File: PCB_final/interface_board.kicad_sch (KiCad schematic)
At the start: 114 parts, among them J1 02x30_Shift_Register_Connector, J2 02x30_ADC_Connector, U1 74HC595, U10 LM321, U2 74HC595, U3 74HC595, U4 74HC595, U5 74HC595, U6 74HC595, U7 74HC595, U8 MAX11643EEG, U9 MAX11643EEG

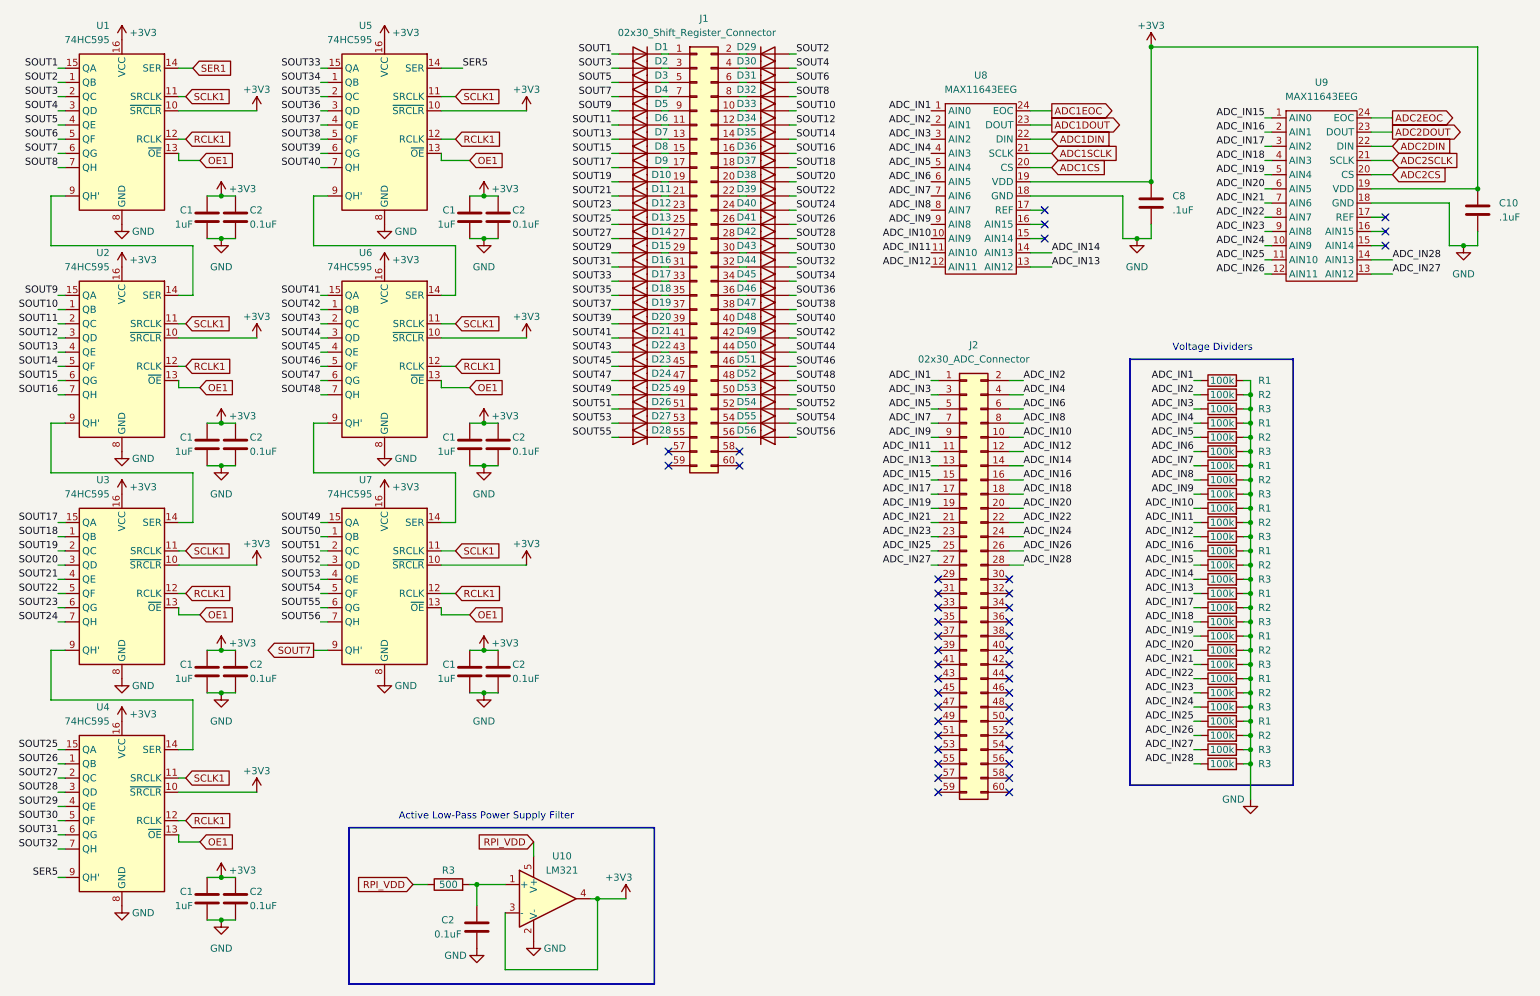
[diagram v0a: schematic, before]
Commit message: Updated op amp and added rpi pico to schematic
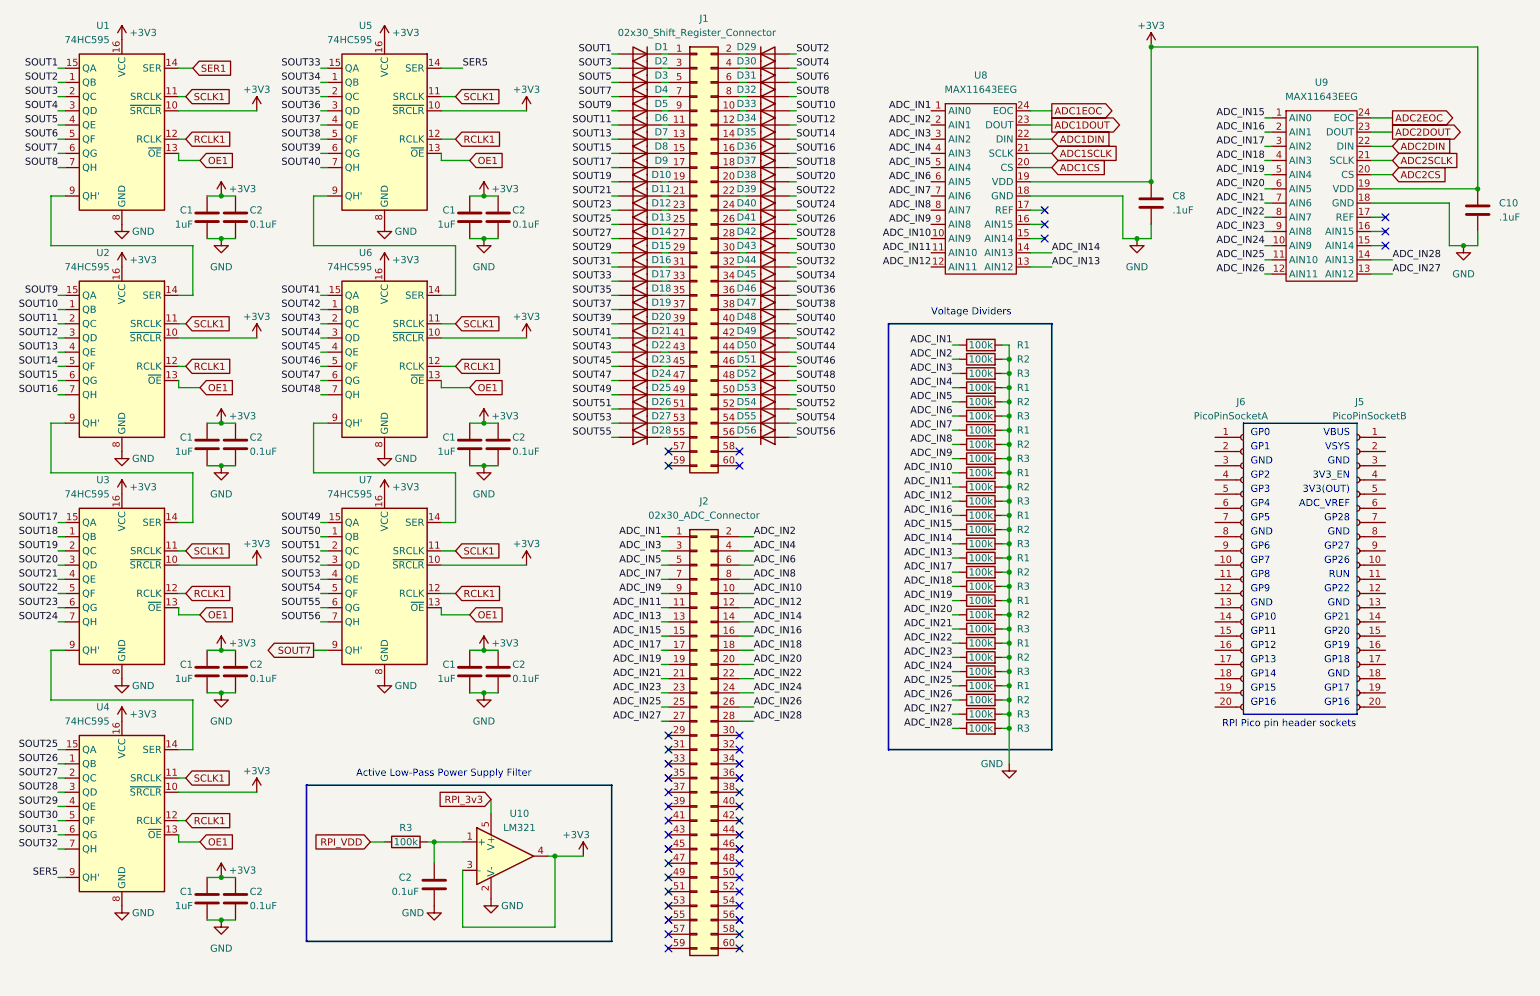
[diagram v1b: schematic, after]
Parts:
- added J5: PicoPinSocketB, symbol Connector:Conn_01x20_Socket
- added J6: PicoPinSocketA, symbol Connector:Conn_01x20_Socket
- R3: value 500 -> 100k
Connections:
- net RPI_VDD: no longer U10.5 (V+)
- new net RPI_3v3: U10.5 (V+)
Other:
- note added: "3V3(OUT)"
- note added: "3V3_EN"
- note added: "ADC_VREF"
- note added: "GND"
- note added: "GP0"
- note added: "GP1"
- note added: "GP10"
- note added: "GP11"
- note added: "GP12"
- note added: "GP13"
- note added: "GP14"
- note added: "GP15"
- note added: "GP16"
- note added: "GP17"
- note added: "GP18"
- note added: "GP19"
- note added: "GP2"
- note added: "GP20"
- note added: "GP21"
- note added: "GP22"
- note added: "GP26"
- note added: "GP27"
- note added: "GP28"
- note added: "GP3"
- note added: "GP4"
- note added: "GP5"
- note added: "GP6"
- note added: "GP7"
- note added: "GP8"
- note added: "GP9"
- note added: "RPI Pico pin header sockets"
- note added: "RUN"
- note added: "VBUS"
- note added: "VSYS"
- moved on the sheet: C2, J2, R1, R2, R3, U10

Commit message: Connected all pins to the pico
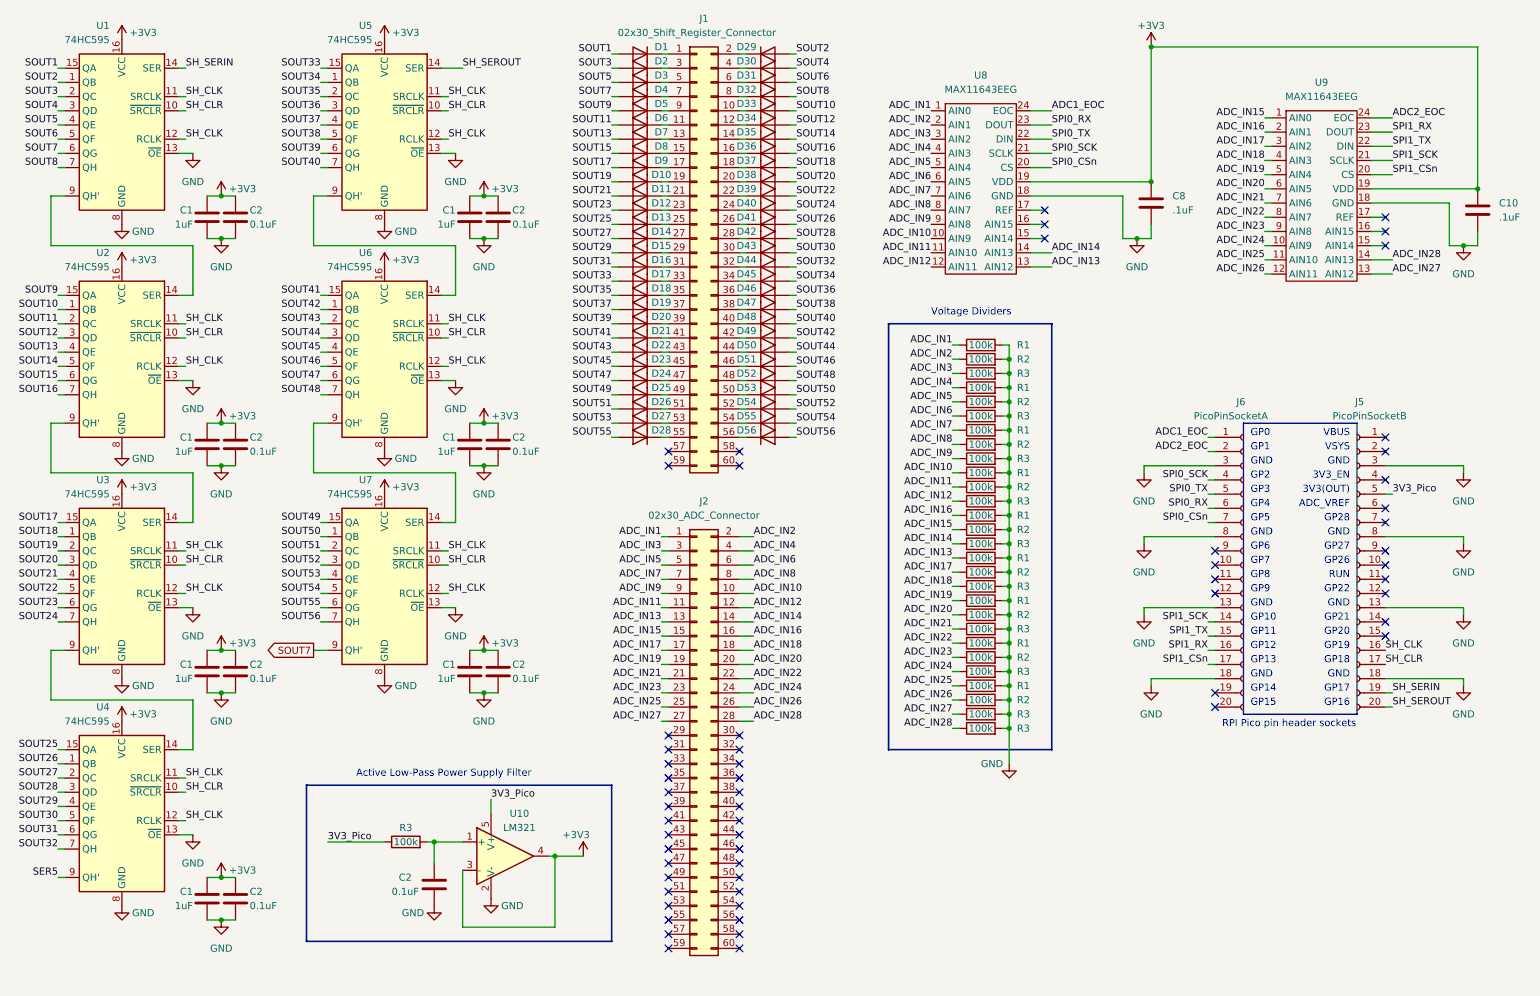
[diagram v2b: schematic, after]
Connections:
- net ADC1CS is gone; now on net SPI0_CSn: U8.20 (CS)
- net ADC1DIN is gone; now on net SPI0_TX: U8.22 (DIN)
- net ADC1DOUT is gone; now on net SPI0_RX: U8.23 (DOUT)
- net ADC1EOC is gone; now on net ADC1_EOC: U8.24 (EOC)
- net ADC1SCLK is gone; now on net SPI0_SCK: U8.21 (SCLK)
- net ADC2CS is gone; now on net SPI1_CSn: U9.20 (CS)
- net ADC2DIN is gone; now on net SPI1_TX: U9.22 (DIN)
- net ADC2DOUT is gone; now on net SPI1_RX: U9.23 (DOUT)
- net ADC2EOC is gone; now on net ADC2_EOC: U9.24 (EOC)
- net ADC2SCLK is gone; now on net SPI1_SCK: U9.21 (SCLK)
- net OE1 is gone; now on net GND: U1.13 (~{OE}), U2.13 (~{OE}), U3.13 (~{OE}), U4.13 (~{OE}), U5.13 (~{OE}), U6.13 (~{OE}), U7.13 (~{OE})
- net RCLK1 is gone; now on net SH_CLK: U1.12 (RCLK), U2.12 (RCLK), U3.12 (RCLK), U4.12 (RCLK), U5.12 (RCLK), U6.12 (RCLK), U7.12 (RCLK)
- net RPI_3v3 is gone; now on net 3V3_Pico: U10.5 (V+)
- net RPI_VDD is gone; now on net 3V3_Pico: R3.1
- net SCLK1 is gone; now on net SH_CLK: U1.11 (SRCLK), U2.11 (SRCLK), U3.11 (SRCLK), U4.11 (SRCLK), U5.11 (SRCLK), U6.11 (SRCLK), U7.11 (SRCLK)
- net SER1 is gone; now on net SH_SERIN: U1.14 (SER)
- net +3V3: no longer U1.10 (~{SRCLR}), U2.10 (~{SRCLR}), U3.10 (~{SRCLR}), U4.10 (~{SRCLR}), U5.10 (~{SRCLR}), U6.10 (~{SRCLR}), U7.10 (~{SRCLR})
- net GND: now also J5.13 (Pin_13), J5.18 (Pin_18), J5.3 (Pin_3), J5.8 (Pin_8), J6.13 (Pin_13), J6.18 (Pin_18), J6.3 (Pin_3), J6.8 (Pin_8)
- net SER5: no longer U5.14 (SER)
- net SH_CLK: now reaches J5.16 (Pin_16)
- net SH_CLR: now reaches J5.17 (Pin_17)
- net SH_CLR: now also U1.10 (~{SRCLR}), U2.10 (~{SRCLR}), U3.10 (~{SRCLR}), U4.10 (~{SRCLR}), U5.10 (~{SRCLR}), U6.10 (~{SRCLR}), U7.10 (~{SRCLR})
- net SH_SERIN: now reaches J5.19 (Pin_19)
- net SH_SEROUT: now reaches J5.20 (Pin_20)
- net SH_SEROUT: now also U5.14 (SER)
- net 3V3_Pico: now reaches J5.5 (Pin_5)
- net ADC1_EOC: now reaches J6.1 (Pin_1)
- net SPI1_SCK: now reaches J6.14 (Pin_14)
- net SPI1_TX: now reaches J6.15 (Pin_15)
- net SPI1_RX: now reaches J6.16 (Pin_16)
- net SPI1_CSn: now reaches J6.17 (Pin_17)
- net ADC2_EOC: now reaches J6.2 (Pin_2)
- net SPI0_SCK: now reaches J6.4 (Pin_4)
- net SPI0_TX: now reaches J6.5 (Pin_5)
- net SPI0_RX: now reaches J6.6 (Pin_6)
- net SPI0_CSn: now reaches J6.7 (Pin_7)
- no-connect marks 42 -> 59
